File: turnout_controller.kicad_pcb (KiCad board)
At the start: 2 copper layers, 25.4 x 12.7 mm, 30 parts, among them J1 DCC_A, J2 DCC_B, J3 PROG, J4 MOT_CNTL, J5 MOT_POWER, J6 MOT_GND, J7 LED_1, J8 LED_2, SW1 SW_Push, SW2 SW_Push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

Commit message: TPS561201 Revision 2
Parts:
- removed the REF** at (86.4, 79.2)
- added REF**: MountingHole_1.2mm, tt_mounting:MountingHole_1.2mm, F.Cu at (109.6, 92.2)
- D3, D4, R5: moved to B.Cu
- SW1, SW2: moved to F.Cu
- moved SW1 28.7 mm to (119.6, 85.9), turned to 0 degrees
- moved D4 25.5 mm to (115.8, 88.2), turned to 0 degrees
- moved C1 23.3 mm to (108.5, 97.9), turned to 180 degrees
- moved C4 21.6 mm to (104.8, 97.9), turned to 180 degrees
- moved J2 18.0 mm to (96.2, 97.4)
- moved U1 18.0 mm to (104.8, 94.8), turned to 90 degrees
- moved D3 17.0 mm to (102.0, 88.2), turned to 0 degrees
- moved J3 15.7 mm to (114.7, 98.7)
- moved J5 15.6 mm to (121.6, 97.8)
- moved J8 15.3 mm to (121.6, 90.8)
- moved J7 14.6 mm to (121.6, 92.4)
- moved J4 14.4 mm to (121.6, 94.8)
- moved SW2 14.3 mm to (101.5, 85.9), turned to 0 degrees
- moved U2 14.2 mm to (114.7, 94.7)
- moved C3 14.0 mm to (109.9, 95.0)
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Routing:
- net /LED1: track 4.93 -> 37.5 mm, vias 0 -> 1
- net 5V: track 27.7 -> 39.6 mm, vias 1 -> 4
- net /LED2: track 35.2 -> 24.2 mm, vias 3 -> 1
- net 12V: track 12.7 -> 21.9 mm, vias 0 -> 2
- net GND: track 17.5 -> 25.9 mm, vias 3 -> 0
- net Net-(R5-Pad1): track 7.07 -> 0.00 mm
- net /KEY_UP: track 22.3 -> 16.0 mm, vias 2 -> 0
- net /KEY_DN: track 18.0 -> 22.6 mm, vias 1 -> 2
- net Net-(C2-Pad2): track 5.91 -> 10.3 mm, vias 0 -> 2
- net Net-(C2-Pad1): track 6.19 -> 1.82 mm
- net Net-(R3-Pad1): track 2.03 -> 6.09 mm
- net Net-(D1-Pad1): track 1.61 -> 5.58 mm
- net /DCC_A: track 10.2 -> 13.0 mm
- net /DCC_B: track 3.12 -> 1.54 mm
- net /SWD_IO: track 5.53 -> 4.01 mm, vias 0 -> 1
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- removed copper zone on B.Cu, net GND
- removed copper zone on F.Cu, net GND
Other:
- outline, holes or cut-outs redrawn

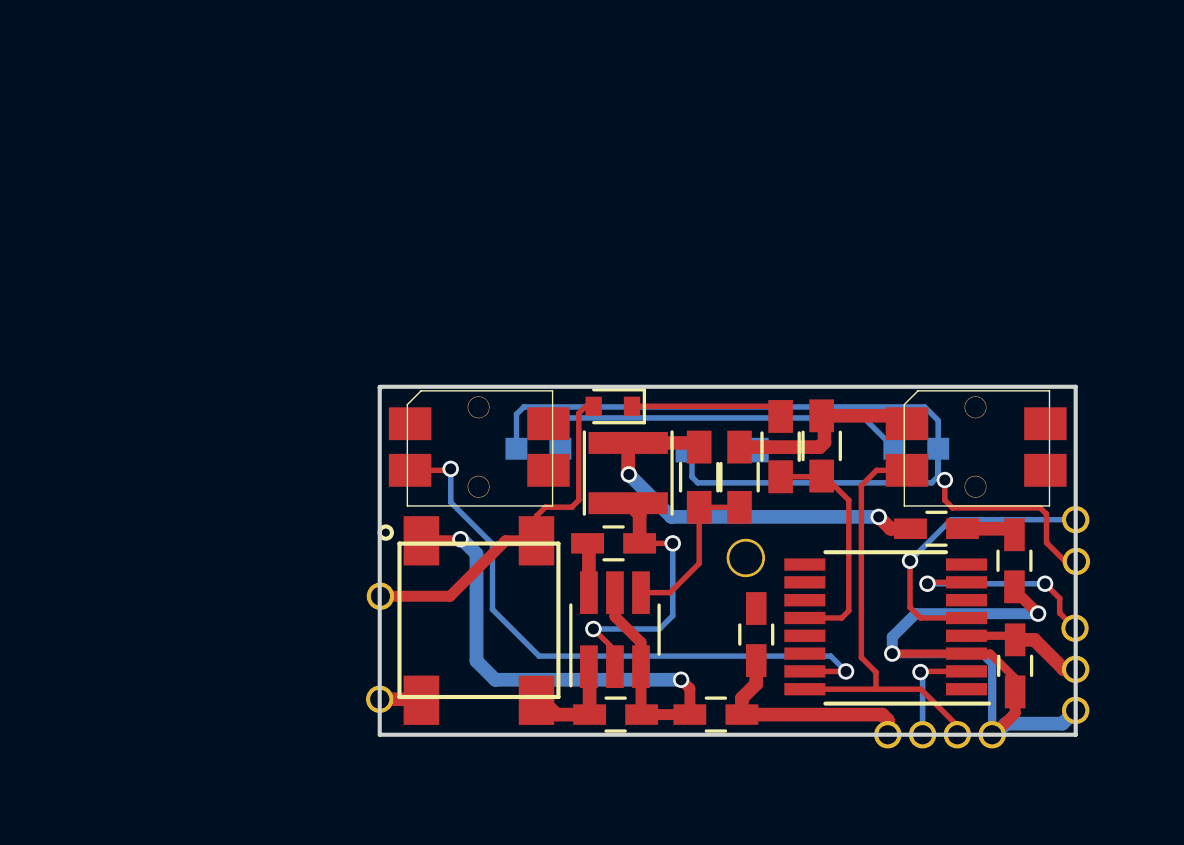
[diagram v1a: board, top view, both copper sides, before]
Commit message: TPS561201 - final board for review
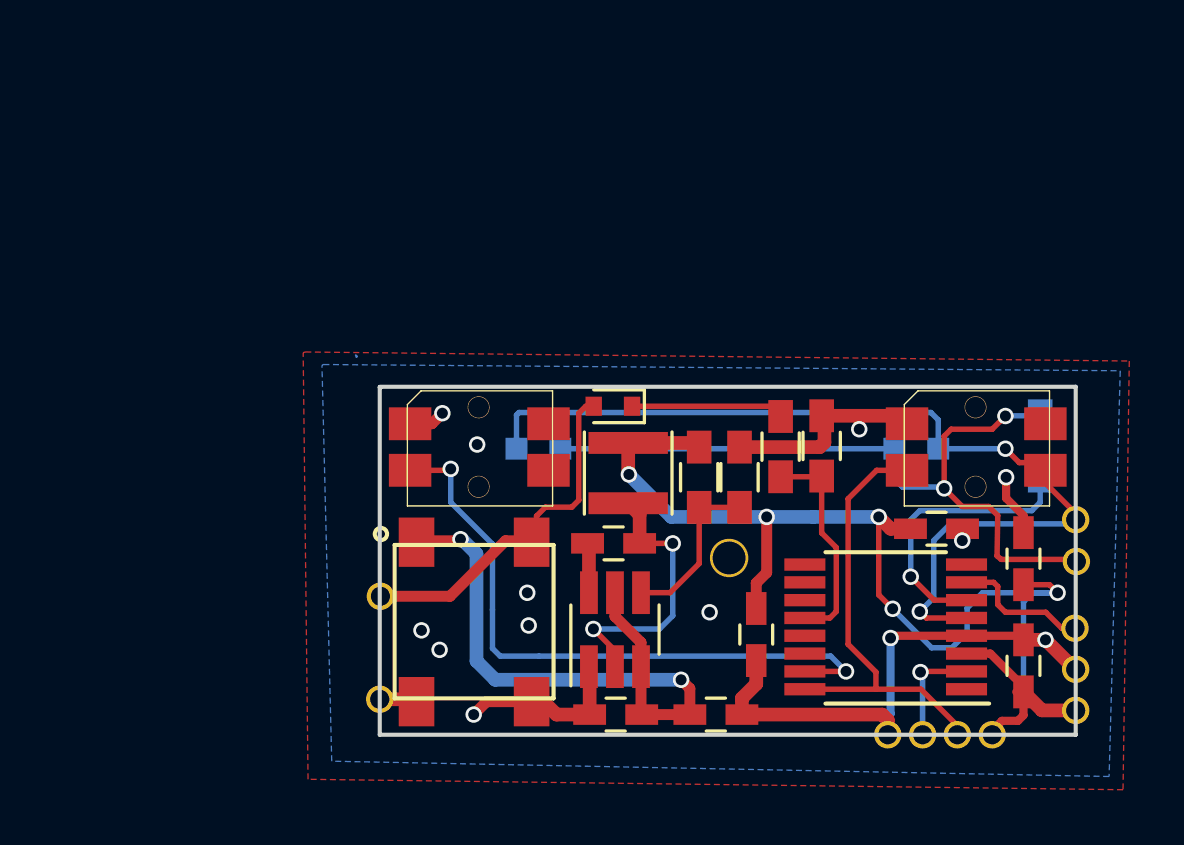
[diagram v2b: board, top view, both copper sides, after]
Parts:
- moved R5 11.6 mm to (120.3, 88.1), turned to 90 degrees
- moved REF** 0.61 mm to (108.9, 92.2)
- moved C6 0.34 mm to (119.7, 92.3)
- moved C7 0.30 mm to (119.7, 96.2)
- moved D2 0.18 mm to (102.1, 95.4)
- turned D3 to 180 degrees
- turned D4 to 180 degrees
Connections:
- SW1 pad 4: (no net) -> /LED2
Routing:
- net GND: track 25.9 -> 38.3 mm, vias 0 -> 13
- net Net-(R5-Pad1): track 0.00 -> 10.9 mm, vias 0 -> 1
- net /LED2: track 24.2 -> 34.8 mm, vias 1 -> 2
- net /LED1: track 37.5 -> 27.8 mm, vias 1 -> 2
- net 5V: track 39.6 -> 45.7 mm, vias 4 -> 5
- net Net-(J4-Pad1): track 7.82 -> 5.04 mm, vias 2 -> 0
- net /KEY_DN: track 22.6 -> 23.4 mm
- net /DCC_IN: track 8.61 -> 7.92 mm
- added copper zone on B.Cu, net GND
- added copper zone on F.Cu, net GND

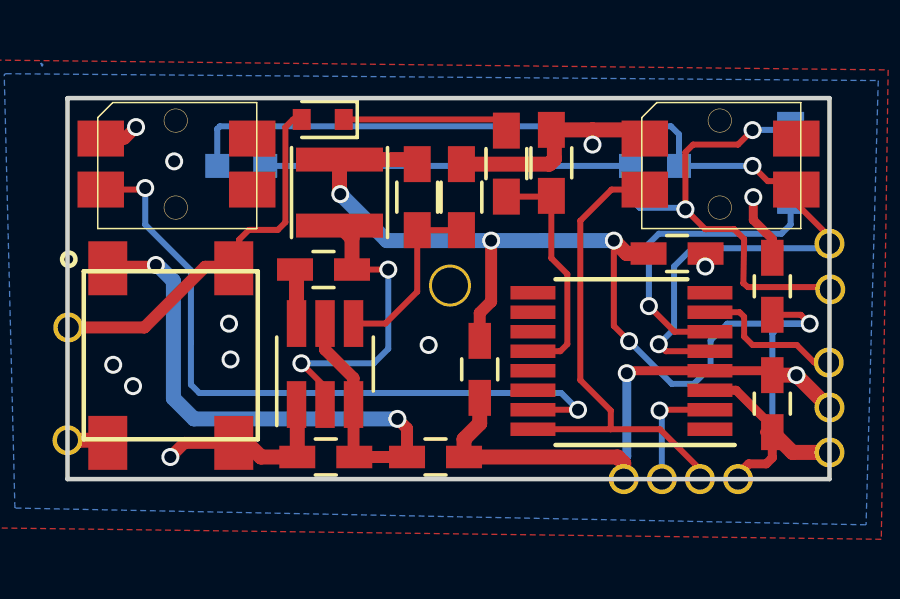
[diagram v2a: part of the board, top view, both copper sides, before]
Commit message: TPS561201 - final board for review - added mounting pads
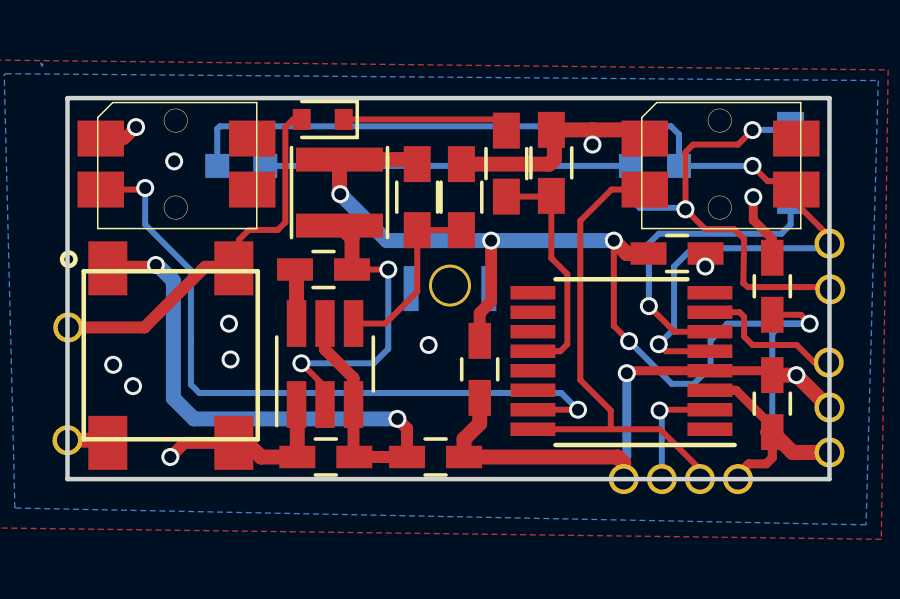
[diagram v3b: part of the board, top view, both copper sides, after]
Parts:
- added REF**: 1pin, tt_mounting:1pad-SMD, B.Cu at (107.6, 92.3)
- added REF**: 1pin, tt_mounting:1pad-SMD, B.Cu at (110.2, 92.3)
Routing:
- net GND: track 38.3 -> 38.0 mm, vias 13 -> 7
- net (no net): track 0.00 -> 0.32 mm, vias 0 -> 6
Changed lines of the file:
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@@
     (tracks 247)
     (zones 0)
-    (modules 30)
+    (modules 32)
     (nets 25)
   )
@@
       (net 1 GND))
   )
+  (module tt_mounting:1pad-SMD (layer B.Cu)
+    (at 107.6452 92.329)
+    (descr "module 1 pin (ou trou mecanique de percage)")
+    (tags DEV)
+    (fp_text reference REF** (at 0 3.048) (layer B.SilkS) hide
+      (effects (font (size 1 1) (thickness 0.15)) (justify mirror))
+    )
+    (fp_text value 1pin (at 0 -3) (layer B.Fab) hide
+      (effects (font (size 1 1) (thickness 0.15)) (justify mirror))
+    )
+    (pad 1 smd rect (at 0 0) (size 0.5 1.5) (layers B.Cu B.Paste B.Mask))
+  )
+  (module tt_mounting:1pad-SMD (layer B.Cu)
+    (at 110.236 92.329)
+    (descr "module 1 pin (ou trou mecanique de percage)")
+    (tags DEV)
+    (fp_text reference REF** (at 0 3.048) (layer B.SilkS) hide
+      (effects (font (size 1 1) (thickness 0.15)) (justify mirror))
+    )
+    (fp_text value 1pin (at 0 -3) (layer B.Fab) hide
+      (effects (font (size 1 1) (thickness 0.15)) (justify mirror))
+    )
+    (pad 1 smd rect (at 0 0) (size 0.5 1.5) (layers B.Cu B.Paste B.Mask))
+  )
   (gr_line (start 96.1898 86.0044) (end 96.2152 86.0044) (angle 90) (layer Edge.Cuts) (width 0.15))
   (gr_line (start 96.1898 98.679) (end 96.1898 86.0044) (angle 90) (layer Edge.Cuts) (width 0.15))
@@
   (gr_line (start 121.5898 85.979) (end 121.5898 98.679) (angle 90) (layer Edge.Cuts) (width 0.15))
   (gr_line (start 96.1898 85.979) (end 121.5898 85.979) (angle 90) (layer Edge.Cuts) (width 0.15))
-  (segment (start 99.695 88.0364) (end 99.7458 88.0872) (width 0.3) (layer B.Cu) (net 1))
-  (via (at 99.7458 88.0872) (size 0.6) (drill 0.4) (layers F.Cu B.Cu) (net 1))
-  (segment (start 108.1786 94.2086) (end 108.2294 94.2086) (width 0.3) (layer F.Cu) (net 1))
-  (via (at 108.2294 94.2086) (size 0.6) (drill 0.4) (layers F.Cu B.Cu) (net 1))
-  (segment (start 101.6508 94.6404) (end 101.6508 94.6658) (width 0.3) (layer B.Cu) (net 1))
-  (via (at 101.6254 94.6912) (size 0.6) (drill 0.4) (layers F.Cu B.Cu) (net 1))
-  (segment (start 101.6508 94.6658) (end 101.6254 94.6912) (width 0.3) (layer B.Cu) (net 1))
-  (segment (start 101.6 93.3958) (end 101.6 93.472) (width 0.3) (layer B.Cu) (net 1))
-  (via (at 101.5746 93.4974) (size 0.6) (drill 0.4) (layers F.Cu B.Cu) (net 1))
-  (segment (start 101.6 93.472) (end 101.5746 93.4974) (width 0.3) (layer B.Cu) (net 1))
-  (segment (start 98.3996 95.5802) (end 98.3742 95.5802) (width 0.3) (layer F.Cu) (net 1))
-  (via (at 98.3742 95.5802) (size 0.6) (drill 0.4) (layers F.Cu B.Cu) (net 1))
-  (via (at 97.7138 94.869) (size 0.6) (drill 0.4) (layers F.Cu B.Cu) (net 1))
+  (segment (start 99.695 88.0364) (end 99.7458 88.0872) (width 0.3) (layer B.Cu) (net 0))
+  (via (at 99.7458 88.0872) (size 0.6) (drill 0.4) (layers F.Cu B.Cu) (net 0))
+  (segment (start 108.1786 94.2086) (end 108.2294 94.2086) (width 0.3) (layer F.Cu) (net 0))
+  (via (at 108.2294 94.2086) (size 0.6) (drill 0.4) (layers F.Cu B.Cu) (net 0))
+  (segment (start 101.6508 94.6404) (end 101.6508 94.6658) (width 0.3) (layer B.Cu) (net 0))
+  (via (at 101.6254 94.6912) (size 0.6) (drill 0.4) (layers F.Cu B.Cu) (net 0))
+  (segment (start 101.6508 94.6658) (end 101.6254 94.6912) (width 0.3) (layer B.Cu) (net 0))
+  (segment (start 101.6 93.3958) (end 101.6 93.472) (width 0.3) (layer B.Cu) (net 0))
+  (via (at 101.5746 93.4974) (size 0.6) (drill 0.4) (layers F.Cu B.Cu) (net 0))
+  (segment (start 101.6 93.472) (end 101.5746 93.4974) (width 0.3) (layer B.Cu) (net 0))
+  (segment (start 98.3996 95.5802) (end 98.3742 95.5802) (width 0.3) (layer F.Cu) (net 0))
+  (via (at 98.3742 95.5802) (size 0.6) (drill 0.4) (layers F.Cu B.Cu) (net 0))
+  (via (at 97.7138 94.869) (size 0.6) (drill 0.4) (layers F.Cu B.Cu) (net 0))
   (segment (start 119.6848 95.2144) (end 120.4874 95.2144) (width 0.3) (layer F.Cu) (net 1))
   (via (at 120.4874 95.2144) (size 0.6) (drill 0.4) (layers F.Cu B.Cu) (net 1))
@@
   (via (at 106.8832 91.694) (size 0.6) (drill 0.4) (layers F.Cu B.Cu) (net 4))
   (segment (start 106.8832 91.694) (end 105.6742 91.694) (width 0.2) (layer F.Cu) (net 4))
-  (segment (start 118.5418 98.679) (end 118.5418 98.5266) (width 0.3) (layer F.Cu) (net 5) (status C00000))
-  (segment (start 118.5418 98.5266) (end 118.8974 98.171) (width 0.3) (layer F.Cu) (net 5) (status 400000))
-  (segment (start 119.6848 97.9678) (end 119.6848 97.1144) (width 0.3) (layer F.Cu) (net 5) (status 800000))
+  (segment (start 118.5418 98.679) (end 118.5418 98.5266) (width 0.3) (layer F.Cu) (net 5))
+  (segment (start 118.5418 98.5266) (end 118.8974 98.171) (width 0.3) (layer F.Cu) (net 5))
+  (segment (start 119.6848 97.9678) (end 119.6848 97.1144) (width 0.3) (layer F.Cu) (net 5))
   (segment (start 119.4816 98.171) (end 119.6848 97.9678) (width 0.3) (layer F.Cu) (net 5))
   (segment (start 118.8974 98.171) (end 119.4816 98.171) (width 0.3) (layer F.Cu) (net 5))

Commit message: Holes replaced with via part using proper via sitching techniques.
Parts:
- added REF**: Via-0.6mm-GND, tt_via:Via-0.6mm-GND, F.Cu at (113.6, 88.1)
- added REF**: Via-0.6mm-GND, tt_via:Via-0.6mm-GND, F.Cu at (97.4, 94.8)
- added REF**: Via-0.6mm-GND, tt_via:Via-0.6mm-GND, F.Cu at (107.9, 94.7)
- added REF**: Via-0.6mm-GND, tt_via:Via-0.6mm-GND, F.Cu at (101.7, 93.5)
- added REF**: Via-0.6mm-GND, tt_via:Via-0.6mm-GND, F.Cu at (98.4, 95.6)
- added REF**: Via-0.6mm-GND, tt_via:Via-0.6mm-GND, F.Cu at (108.6, 93.8)
- added REF**: Via-0.6mm-GND, tt_via:Via-0.6mm-GND, F.Cu at (99.8, 88.1)
- added REF**: Via-0.6mm-GND, tt_via:Via-0.6mm-GND, F.Cu at (101.7, 94.7)
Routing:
- net GND: track 38.0 -> 33.9 mm, vias 7 -> 4
- net /LED1: track 27.8 -> 28.8 mm
- net (no net): track 0.32 -> 0.00 mm, vias 6 -> 0
